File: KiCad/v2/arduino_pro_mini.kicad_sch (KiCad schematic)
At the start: 35 parts, among them IC101 ATMEGA328P-AU, J101 Conn_01x06_Pin, J102 Conn_01x15_Pin, J103 Conn_01x15_Pin, SW101 SW_Omron_B3FS, U101 SPX3819M5-L-5-0/TR, U102 SPX3819M5-L-3-3/TR, Y101 16Mhz

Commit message: Initial signal routing
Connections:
- net +3V3: now also R103.1
- net +3V3_LDO: no longer R103.1
- net +5V: now also R101.1
- net +5V_LDO: no longer R101.1
- net D13_SCK: now also R104.1; no longer D105.2 (A)
- net GND: now also D105.1 (K); no longer R104.2
- new net: D105.2 (A), R104.2
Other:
- moved on the sheet: D102, D104, D105, R101, R103, R104

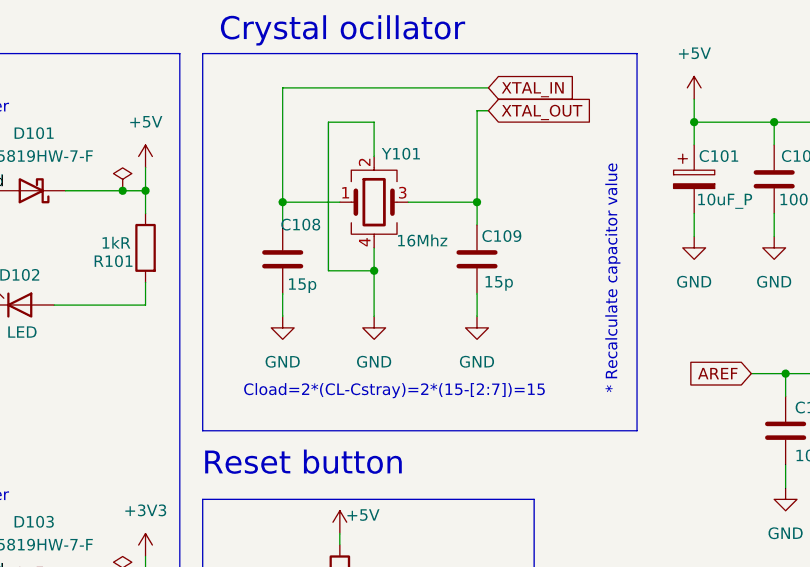
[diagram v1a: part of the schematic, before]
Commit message: Update crystal oscillator
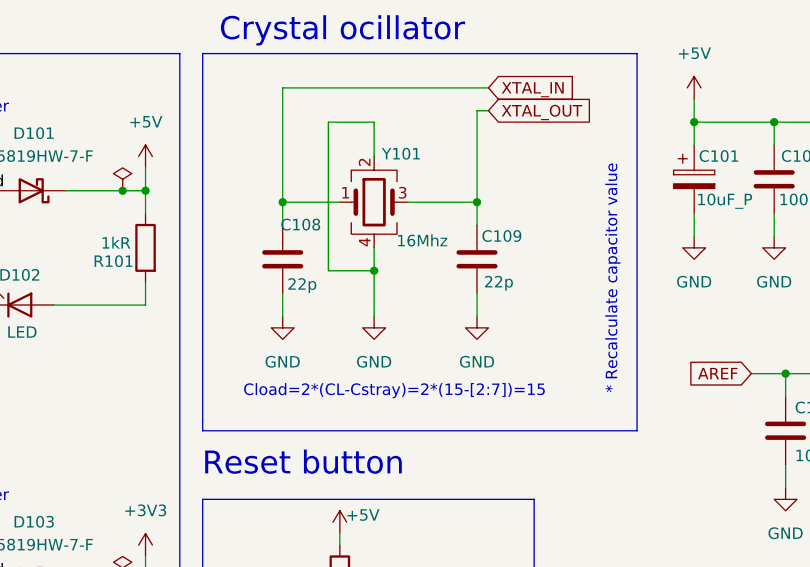
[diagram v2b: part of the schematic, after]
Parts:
- C108, C109: value 15p -> 22p; Manufacturer Part Number CC0603JRNPO9BN150 -> CC0603JRNPO9BN220
- Y101: Manufacturer Part Number X322516MOB4SI -> X322516MRB4SI
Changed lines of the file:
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@@
 			)
 		)
-		(property "Value" "15p"
+		(property "Value" "22p"
 			(at 146.558 48.514 0)
 			(effects
@@
 			)
 		)
-		(property "Manufacturer Part Number" "CC0603JRNPO9BN150"
+		(property "Manufacturer Part Number" "CC0603JRNPO9BN220"
 			(at 146.05 45.72 0)
 			(effects
@@
 			)
 		)
-		(property "Value" "15p"
+		(property "Value" "22p"
 			(at 168.402 48.26 0)
 			(effects
@@
 			)
 		)
-		(property "Manufacturer Part Number" "CC0603JRNPO9BN150"
+		(property "Manufacturer Part Number" "CC0603JRNPO9BN220"
 			(at 167.64 45.72 0)
 			(effects
@@
 			)
 		)
-		(property "Manufacturer Part Number" "X322516MOB4SI"
+		(property "Manufacturer Part Number" "X322516MRB4SI"
 			(at 156.21 39.37 0)
 			(effects
